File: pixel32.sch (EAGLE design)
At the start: 78 parts, among them CON1 B7B-PH-K-S-SIDE, CON10 PINHEAD_1X01-2.54, CON11 PINHEAD_1X01-2.54, CON12 PINHEAD_1X02-2.54, CON13 PINHEAD_1X07-2, CON14 PINHEAD_1X07-2, CON2 B7B-PH-K-S-SIDE, CON3 PINHEAD_1X02-2.54, CON4 PINHEAD_1X01-2.54, CON5 PINHEAD_1X01-2.54, CON6 PINHEAD_1X01-2.54, CON7 PINHEAD_1X01-2.54, CON8 PINHEAD_1X01-2.54, CON9 PINHEAD_1X01-2.54, IC1 STM32F030K6TX-LQFP32(7X7), IC3 ST3485SOIC8, IC6 MC74VHC1GT125, IC7 MC74VHC1GT125, IC8 LM317, Y1 16MHz

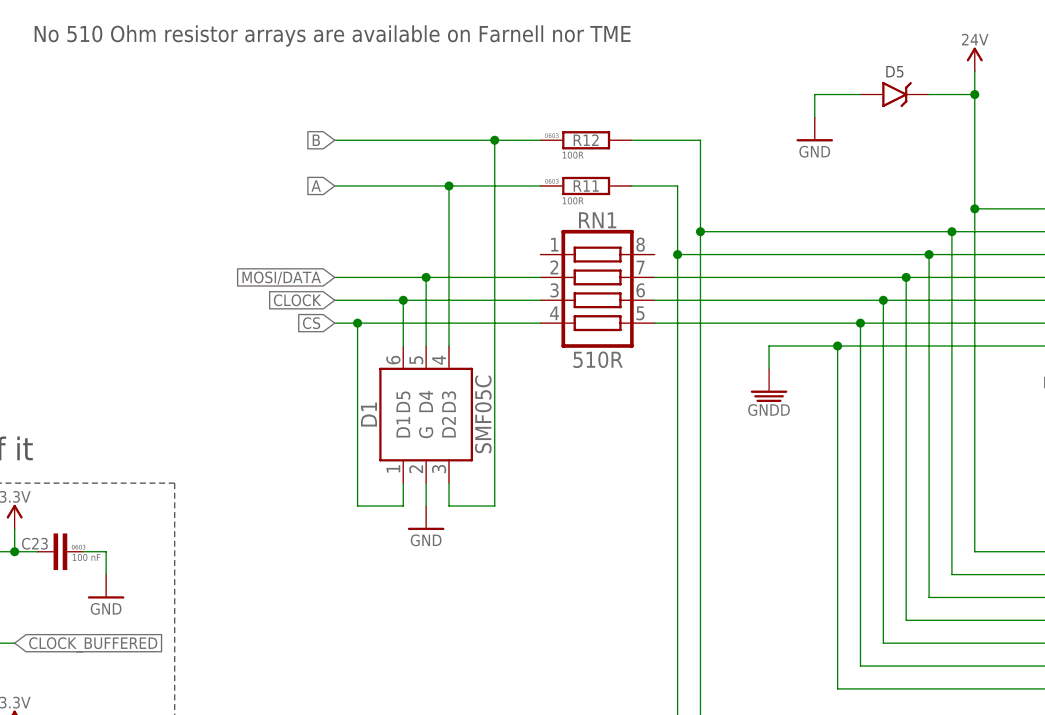
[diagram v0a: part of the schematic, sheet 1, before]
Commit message: Reset pad routing, clearance error resolving
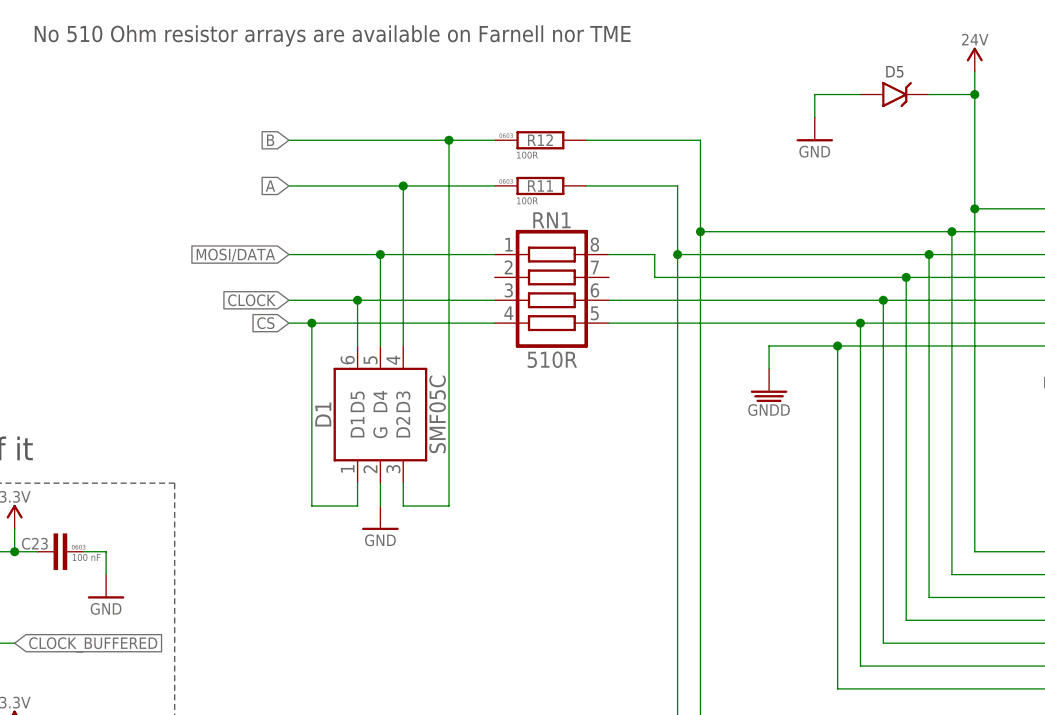
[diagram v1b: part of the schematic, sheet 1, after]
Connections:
- net MOSI/DATA: now also RN1.1; no longer RN1.2
- net N$11: now also RN1.8; no longer RN1.7
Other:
- moved on the sheet: D1, R11, R12, RN1

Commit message: Minor changes
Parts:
- C15: TME# C0603C103K3RACTU -> C0603C103K3RAC
- D5: TME# SMBJ26CA -> SMBJ26CA-LF
- R10: TME# RC0603FR-07100KL -> RC0603FR-07100K
- R11, R12: TME# RC0603FR-07100RL -> RC0603FR-07100R
- R13, R14, R15, R3, R8, R9: TME# RC0603FR-0710KL -> RC0603FR-0710K
- R39, R6: TME# RC0603FR-071KL -> RC0603FR-071K
- R7: TME# RC0603FR-071K6L -> RC0603FR-071K6
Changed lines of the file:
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@@
 </part>
 <part name="R2" library="rc" deviceset="R" device="-R1206" value="2R">
-<attribute name="FARNELL#" value="2328120"/>
-<attribute name="TME#" value="RC1206FR-072RL"/>
+<attribute name="FARNELL#" value="2502621"/>
+<attribute name="TME#" value="RC1206FR-072R"/>
 </part>
 <part name="D1" library="pixel_masterlib" deviceset="DIODE" device="-SOD123">
@@
 <part name="C2" library="rc" deviceset="C" device="-0805" value="1 uF">
 <attribute name="FARNELL#" value="1735541"/>
-<attribute name="TME#" value="GRM21BR71H105KA12K"/>
+<attribute name="TME#" value="GRM21BR71H105KA12L"/>
 </part>
 <part name="GND18" library="supply_symbols" deviceset="GND" device="" value="GND"/>
@@
 <part name="R39" library="rc" deviceset="R" device="-0603" value="1K">
 <attribute name="FARNELL#" value="2303145"/>
-<attribute name="TME#" value="RC0603FR-071KL"/>
+<attribute name="TME#" value="RC0603FR-071K"/>
 </part>
 <part name="IC1" library="pixel_masterlib" deviceset="STM32F030K6TX" device="-LQFP32(7X7)"/>
@@
 <part name="C15" library="rc" deviceset="C" device="-0603" value="10 nF">
 <attribute name="FARNELL#" value="2496827"/>
-<attribute name="TME#" value="C0603C103K3RACTU"/>
+<attribute name="TME#" value="C0603C103K3RAC"/>
 </part>
 <part name="GND5" library="supply_symbols" deviceset="GND" device="" value="GND"/>
@@
 <part name="R11" library="rc" deviceset="R" device="-0603" value="100R">
 <attribute name="FARNELL#" value="2303059"/>
-<attribute name="TME#" value="RC0603FR-07100RL"/>
+<attribute name="TME#" value="RC0603FR-07100R"/>
 </part>
 <part name="R12" library="rc" deviceset="R" device="-0603" value="100R">
 <attribute name="FARNELL#" value="2303059"/>
-<attribute name="TME#" value="RC0603FR-07100RL"/>
+<attribute name="TME#" value="RC0603FR-07100R"/>
 </part>
 <part name="GND26" library="supply_symbols" deviceset="GND" device="" value="GND"/>
@@
 <part name="R8" library="rc" deviceset="R" device="-0603" value="10K">
 <attribute name="FARNELL#" value="2008341"/>
-<attribute name="TME#" value="RC0603FR-0710KL"/>
+<attribute name="TME#" value="RC0603FR-0710K"/>
 </part>
 <part name="CON3" library="pinhead" deviceset="PINHEAD_1X02" device="-2.54"/>
@@
 <part name="R10" library="rc" deviceset="R" device="-0603" value="100K">
 <attribute name="FARNELL#" value="2303232"/>
-<attribute name="TME#" value="RC0603FR-07100KL"/>
+<attribute name="TME#" value="RC0603FR-07100K"/>
 </part>
 <part name="R13" library="rc" deviceset="R" device="-0603" value="10K">
 <attribute name="FARNELL#" value="2008341"/>
-<attribute name="TME#" value="RC0603FR-0710KL"/>
+<attribute name="TME#" value="RC0603FR-0710K"/>
 </part>
 <part name="GND37" library="supply_symbols" deviceset="GND" device="" value="GND"/>
@@
 <part name="R6" library="rc" deviceset="R" device="-0603" value="1K">
 <attribute name="FARNELL#" value="2303145"/>
-<attribute name="TME#" value="RC0603FR-071KL"/>
+<attribute name="TME#" value="RC0603FR-071K"/>
 </part>
 <part name="R7" library="rc" deviceset="R" device="-0603" value="1K6">
 <attribute name="FARNELL#" value="2303159"/>
-<attribute name="TME#" value="RC0603FR-071K6L"/>
+<attribute name="TME#" value="RC0603FR-071K6"/>
 </part>
 <part name="GND30" library="supply_symbols" deviceset="GND" device="" value="GND"/>
@@
 <part name="R9" library="rc" deviceset="R" device="-0603" value="10K">
 <attribute name="FARNELL#" value="2008341"/>
-<attribute name="TME#" value="RC0603FR-0710KL"/>
+<attribute name="TME#" value="RC0603FR-0710K"/>
 </part>
 <part name="GND27" library="supply_symbols" deviceset="GND" device="" value="GND"/>
 <part name="R14" library="rc" deviceset="R" device="-0603" value="10K">
 <attribute name="FARNELL#" value="2008341"/>
-<attribute name="TME#" value="RC0603FR-0710KL"/>
+<attribute name="TME#" value="RC0603FR-0710K"/>
 </part>
 <part name="GND28" library="supply_symbols" deviceset="GND" device="" value="GND"/>
 <part name="R15" library="rc" deviceset="R" device="-0603" value="10K">
 <attribute name="FARNELL#" value="2008341"/>
-<attribute name="TME#" value="RC0603FR-0710KL"/>
+<attribute name="TME#" value="RC0603FR-0710K"/>
 </part>
 <part name="GND42" library="supply_symbols" deviceset="GND" device="" value="GND"/>
@@
 <attribute name="MANF" value="STMicroelectronics"/>
 <attribute name="MANF#" value="SMBJ26CA"/>
-<attribute name="TME#" value="SMBJ26CA"/>
+<attribute name="TME#" value="SMBJ26CA-LF"/>
 </part>
 <part name="GND11" library="supply_symbols" deviceset="GND" device="" value="GND"/>
@@
 <part name="R3" library="rc" deviceset="R" device="-0603" value="10K">
 <attribute name="FARNELL#" value="2008341"/>
-<attribute name="TME#" value="RC0603FR-0710KL"/>
+<attribute name="TME#" value="RC0603FR-0710K"/>
 </part>
 <part name="GND15" library="supply_symbols" deviceset="GND" device="" value="GND"/>

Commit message: Minor changes
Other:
- note removed: "R10, R13 are not defined"
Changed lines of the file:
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@@
 <text x="20.32" y="236.22" size="1.778" layer="97">Crystal load capacitance is 9 pF,
 otherwise recalculate C19 and C20</text>
-<text x="170.18" y="68.58" size="1.778" layer="97">R10, R13 are not defined</text>
 <text x="309.88" y="251.46" size="1.778" layer="97" rot="R180">No 510 Ohm resistor arrays are available on Farnell nor TME</text>
 </plain>

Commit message: minor updates
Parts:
- added SJ5: (no value), eth_conv_master_lib:SOLDER_JOINT
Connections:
- net RX: now also SJ5.2
- net TX: now also SJ5.1
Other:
- note added: "SJ5 is for educational purposes only. DO NOT SHORT IT"
- moved on the sheet: CON8, CON9
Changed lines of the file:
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@@
+<attribute name="BOM" value="EXCLUDE"/>
+</part>
+<part name="SJ5" library="eth_conv_master_lib" deviceset="SOLDER_JOINT" device="">
 <attribute name="BOM" value="EXCLUDE"/>
 </part>
@@
 otherwise recalculate C19 and C20</text>
 <text x="309.88" y="251.46" size="1.778" layer="97" rot="R180">No 510 Ohm resistor arrays are available on Farnell nor TME</text>
+<text x="38.1" y="162.56" size="1.778" layer="97">SJ5 is for educational purposes only. DO NOT SHORT IT</text>
 </plain>
 <moduleinsts>
@@
 <attribute name="BOM" x="129.54" y="228.6" size="1.778" layer="96" display="off"/>
 </instance>
-<instance part="CON8" gate="G$1" x="101.6" y="104.14" rot="R90"/>
-<instance part="CON9" gate="G$1" x="109.22" y="104.14" rot="R90"/>
+<instance part="CON8" gate="G$1" x="101.6" y="101.6" rot="R90"/>
+<instance part="CON9" gate="G$1" x="109.22" y="101.6" rot="R90"/>
 <instance part="CON10" gate="G$1" x="116.84" y="45.72" rot="R90"/>
 <instance part="CON11" gate="G$1" x="124.46" y="45.72" rot="R90"/>
@@
 <instance part="PAD5" gate="G$1" x="114.3" y="238.76" rot="R180">
 <attribute name="BOM" x="114.3" y="238.76" size="1.778" layer="96" rot="R180" display="off"/>
+</instance>
+<instance part="SJ5" gate="G$1" x="60.96" y="175.26" rot="R270">
+<attribute name="BOM" x="60.96" y="175.26" size="1.778" layer="96" rot="R270" display="off"/>
 </instance>
 </instances>
@@
 <wire x1="60.96" y1="198.12" x2="60.96" y2="185.42" width="0.1524" layer="91"/>
 <wire x1="60.96" y1="185.42" x2="45.72" y2="185.42" width="0.1524" layer="91"/>
+<pinref part="SJ5" gate="G$1" pin="1"/>
+<wire x1="60.96" y1="185.42" x2="60.96" y2="180.34" width="0.1524" layer="91"/>
+<junction x="60.96" y="185.42"/>
 </segment>
 <segment>
@@
 <wire x1="76.2" y1="185.42" x2="76.2" y2="182.88" width="0.1524" layer="91"/>
 <wire x1="76.2" y1="182.88" x2="45.72" y2="182.88" width="0.1524" layer="91"/>
+<pinref part="SJ5" gate="G$1" pin="2"/>
+<wire x1="60.96" y1="170.18" x2="60.96" y2="167.64" width="0.1524" layer="91"/>
+<wire x1="60.96" y1="167.64" x2="76.2" y2="167.64" width="0.1524" layer="91"/>
+<wire x1="76.2" y1="167.64" x2="76.2" y2="182.88" width="0.1524" layer="91"/>
+<junction x="76.2" y="182.88"/>
 </segment>
 <segment>
@@
 <junction x="99.06" y="124.46"/>
 <pinref part="CON8" gate="G$1" pin="1"/>
-<wire x1="99.06" y1="111.76" x2="99.06" y2="124.46" width="0.1524" layer="91"/>
+<wire x1="99.06" y1="109.22" x2="99.06" y2="124.46" width="0.1524" layer="91"/>
 </segment>
 </net>
@@
 <junction x="106.68" y="114.3"/>
 <pinref part="CON9" gate="G$1" pin="1"/>
-<wire x1="106.68" y1="111.76" x2="106.68" y2="114.3" width="0.1524" layer="91"/>
-</segment>
-</net>
+<wire x1="106.68" y1="109.22" x2="106.68" y2="114.3" width="0.1524" layer="91"/>
+</segment>
+</net>

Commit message: Minor fixes
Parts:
- added U$10, U$7, U$8, U$9: CONNECTION, usb2can_master_lib:CONNECTION
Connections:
- net GND: now also U$10.P$2, U$7.P$2, U$8.P$2, U$9.P$2
- net GNDD: now also U$10.P$1, U$7.P$1, U$8.P$1, U$9.P$1
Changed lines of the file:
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@@
 <attribute name="BOM" value="EXCLUDE"/>
 </part>
+<part name="U$7" library="usb2can_master_lib" deviceset="CONNECTION" device=""/>
+<part name="U$8" library="usb2can_master_lib" deviceset="CONNECTION" device=""/>
+<part name="U$9" library="usb2can_master_lib" deviceset="CONNECTION" device=""/>
+<part name="U$10" library="usb2can_master_lib" deviceset="CONNECTION" device=""/>
 </parts>
 <sheets>
@@
 </instance>
 <instance part="GND42" gate="1" x="38.1" y="43.18" rot="MR0"/>
-<instance part="U$6" gate="G$1" x="294.64" y="114.3" rot="MR0"/>
-<instance part="GND43" gate="G$1" x="299.72" y="109.22" rot="MR0"/>
-<instance part="GND44" gate="1" x="289.56" y="109.22" rot="MR0"/>
+<instance part="U$6" gate="G$1" x="297.18" y="93.98" rot="MR0"/>
+<instance part="GND43" gate="G$1" x="302.26" y="88.9" rot="MR0"/>
+<instance part="GND44" gate="1" x="292.1" y="88.9" rot="MR0"/>
 <instance part="GND22" gate="G$1" x="325.12" y="134.62" rot="MR0"/>
 <instance part="GND23" gate="G$1" x="325.12" y="210.82" rot="MR0"/>
@@
 <instance part="CON7" gate="G$1" x="119.38" y="139.7" rot="R270"/>
 <instance part="+P18" gate="G$1" x="109.22" y="190.5"/>
-<instance part="U$3" gate="G$1" x="294.64" y="116.84" rot="MR0"/>
+<instance part="U$3" gate="G$1" x="297.18" y="96.52" rot="MR0"/>
 <instance part="PAD3" gate="G$1" x="129.54" y="228.6">
 <attribute name="BOM" x="129.54" y="228.6" size="1.778" layer="96" display="off"/>
@@
 <attribute name="BOM" x="60.96" y="175.26" size="1.778" layer="96" rot="R270" display="off"/>
 </instance>
+<instance part="U$7" gate="G$1" x="297.18" y="99.06" rot="MR0"/>
+<instance part="U$8" gate="G$1" x="297.18" y="101.6" rot="MR0"/>
+<instance part="U$9" gate="G$1" x="297.18" y="104.14" rot="MR0"/>
+<instance part="U$10" gate="G$1" x="297.18" y="106.68" rot="MR0"/>
 </instances>
 <busses>
@@
 <segment>
 <pinref part="U$6" gate="G$1" pin="P$2"/>
-<wire x1="292.1" y1="114.3" x2="289.56" y2="114.3" width="0.1524" layer="91"/>
+<wire x1="294.64" y1="93.98" x2="292.1" y2="93.98" width="0.1524" layer="91"/>
 <pinref part="GND44" gate="1" pin="GND"/>
-<wire x1="289.56" y1="114.3" x2="289.56" y2="111.76" width="0.1524" layer="91"/>
-<wire x1="289.56" y1="114.3" x2="289.56" y2="116.84" width="0.1524" layer="91"/>
-<junction x="289.56" y="114.3"/>
+<wire x1="292.1" y1="93.98" x2="292.1" y2="91.44" width="0.1524" layer="91"/>
+<wire x1="292.1" y1="93.98" x2="292.1" y2="96.52" width="0.1524" layer="91"/>
+<junction x="292.1" y="93.98"/>
 <pinref part="U$3" gate="G$1" pin="P$2"/>
-<wire x1="292.1" y1="116.84" x2="289.56" y2="116.84" width="0.1524" layer="91"/>
+<wire x1="294.64" y1="96.52" x2="292.1" y2="96.52" width="0.1524" layer="91"/>
+<pinref part="U$9" gate="G$1" pin="P$2"/>
+<wire x1="294.64" y1="104.14" x2="292.1" y2="104.14" width="0.1524" layer="91"/>
+<wire x1="292.1" y1="104.14" x2="292.1" y2="101.6" width="0.1524" layer="91"/>
+<junction x="292.1" y="96.52"/>
+<pinref part="U$7" gate="G$1" pin="P$2"/>
+<wire x1="292.1" y1="101.6" x2="292.1" y2="99.06" width="0.1524" layer="91"/>
+<wire x1="292.1" y1="99.06" x2="292.1" y2="96.52" width="0.1524" layer="91"/>
+<wire x1="294.64" y1="99.06" x2="292.1" y2="99.06" width="0.1524" layer="91"/>
+<junction x="292.1" y="99.06"/>
+<pinref part="U$8" gate="G$1" pin="P$2"/>
+<wire x1="294.64" y1="101.6" x2="292.1" y2="101.6" width="0.1524" layer="91"/>
+<junction x="292.1" y="101.6"/>
+<pinref part="U$10" gate="G$1" pin="P$2"/>
+<wire x1="294.64" y1="106.68" x2="292.1" y2="106.68" width="0.1524" layer="91"/>
+<wire x1="292.1" y1="106.68" x2="292.1" y2="104.14" width="0.1524" layer="91"/>
+<junction x="292.1" y="104.14"/>
 </segment>
 <segment>
@@
 <segment>
 <pinref part="GND43" gate="G$1" pin="GNDD"/>
-<wire x1="299.72" y1="111.76" x2="299.72" y2="114.3" width="0.1524" layer="91"/>
+<wire x1="302.26" y1="91.44" x2="302.26" y2="93.98" width="0.1524" layer="91"/>
 <pinref part="U$6" gate="G$1" pin="P$1"/>
-<wire x1="299.72" y1="114.3" x2="297.18" y2="114.3" width="0.1524" layer="91"/>
+<wire x1="302.26" y1="93.98" x2="299.72" y2="93.98" width="0.1524" layer="91"/>
 <pinref part="U$3" gate="G$1" pin="P$1"/>
-<wire x1="297.18" y1="116.84" x2="299.72" y2="116.84" width="0.1524" layer="91"/>
-<wire x1="299.72" y1="116.84" x2="299.72" y2="114.3" width="0.1524" layer="91"/>
-<junction x="299.72" y="114.3"/>
-</segment>
-<segment>
+<wire x1="299.72" y1="96.52" x2="302.26" y2="96.52" width="0.1524" layer="91"/>
+<wire x1="302.26" y1="96.52" x2="302.26" y2="93.98" width="0.1524" layer="91"/>
+<junction x="302.26" y="93.98"/>
+<pinref part="U$9" gate="G$1" pin="P$1"/>
+<wire x1="299.72" y1="104.14" x2="302.26" y2="104.14" width="0.1524" layer="91"/>
+<wire x1="302.26" y1="104.14" x2="302.26" y2="101.6" width="0.1524" layer="91"/>
+<junction x="302.26" y="96.52"/>
+<pinref part="U$8" gate="G$1" pin="P$1"/>
+<wire x1="302.26" y1="101.6" x2="302.26" y2="99.06" width="0.1524" layer="91"/>
+<wire x1="302.26" y1="99.06" x2="302.26" y2="96.52" width="0.1524" layer="91"/>
+<wire x1="299.72" y1="101.6" x2="302.26" y2="101.6" width="0.1524" layer="91"/>
+<junction x="302.26" y="101.6"/>
+<pinref part="U$7" gate="G$1" pin="P$1"/>
+<wire x1="299.72" y1="99.06" x2="302.26" y2="99.06" width="0.1524" layer="91"/>
+<junction x="302.26" y="99.06"/>
+<pinref part="U$10" gate="G$1" pin="P$1"/>
+<wire x1="299.72" y1="106.68" x2="302.26" y2="106.68" width="0.1524" layer="91"/>
+<wire x1="302.26" y1="106.68" x2="302.26" y2="104.14" width="0.1524" layer="91"/>
+<junction x="302.26" y="104.14"/>
+</segment>
+<segment>
